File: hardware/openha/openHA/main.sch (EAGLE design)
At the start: 58 parts, among them U1 STM32L476JX, U2 PCM1774RGPR, U3 STC3115IQT, X1 ABS06-107SMT, X2 ABS06-107SMT

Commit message: Initial corrections
Miscellaneous corrections of the initial commit
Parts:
- removed U$1: BATT, STM32:BATT
- removed U$15: BLUENRG-MS, STM32:BLUENRG-MS
- removed U$16: BALF-NRG-01D3, STM32:BALF-NRG-01D3
- removed U$17: ANT, STM32:ANT
- removed U$18, U$19: 2k, STM32:RESISTOR
- removed U$2: USB, STM32:USB
- removed U$3: LD5115J18, STM32:LD5115J18
- removed U$4: STBC08, STM32:STBC08
- removed U$5: USBLC6-2, STM32:USBLC6-2
- removed U$7: MP34DT05-A, STM32:MP34DT05-A
- removed U$8: LDK130, STM32:LDK130
- removed X1, X2: ABS06-107SMT, STM32:ABS06-107SMT
- added A1: ANT, OAlib:ANT
- added C37, C38: 4.7uF, OAlib:CAP0603
- added J1: 2PIN, OAlib:2PIN
- added J2: BATT, OAlib:BATT
- added J3: CS44, OAlib:CS44
- added L2: 3.9NH, SparkFun-Coils:INDUCTOR-0402-3.9NH
- added R3: 2k, OAlib:RESISTOR
- added R4: 0R, OAlib:RESISTOR
- added R5: 20k, OAlib:RESISTOR
- added S2: SW_DPDT, OAlib:SW_DPDT
- added U10: STBC08, OAlib:STBC08
- added U4: PCM1774RGPR, PCM1774:PCM1774RGPR
- added U5: BLUENRG-MS, OAlib:BLUENRG-MS
- added U6: LD39115J18, OAlib:LD39115J18
- added U7: STC3115IQT, STC3115IQT:STC3115IQT
- added U8: USBLC6-2, OAlib:USBLC6-2
- added U9: LDK130, OAlib:LDK130
- added Y1, Y2: ABS06-107SMT, OAlib:ABS06-107SMT
- C1, C11, C12, C17, C18, C19, C21, C22, C23, C24, C25, C3, C7, C8: device STM32:CAP0603 -> OAlib:CAP0603
- C10, C34, C6, C9: value 4.7uF -> 1uF; device STM32:CAP0603 -> OAlib:CAP0603
- C13: value 1uF -> 100nF; device STM32:CAP0603 -> OAlib:CAP0603
- C14, C15, C16: value 1uF -> 4.7uF; device STM32:CAP0603 -> OAlib:CAP0603
- C2: value 4pF -> 1uF; device STM32:CAP0603 -> OAlib:CAP0603
- C20: value 4.7uF -> 100pF; device STM32:CAP0603 -> OAlib:CAP0603
- C26: value 150nF -> 15pF; device STM32:CAP0603 -> OAlib:CAP0603
- C27: value 100p -> 150nF; device STM32:CAP0603 -> OAlib:CAP0603
- C28: value 100nF -> 100p; device STM32:CAP0603 -> OAlib:CAP0603
- C29: value 1uF -> 15pF; device STM32:CAP0603 -> OAlib:CAP0603
- C30: value 100pF -> 100nF; device STM32:CAP0603 -> OAlib:CAP0603
- C31, C4: value 100nF -> 1uF; device STM32:CAP0603 -> OAlib:CAP0603
- C32: value 1uF -> 4pF; device STM32:CAP0603 -> OAlib:CAP0603
- C33, C5: value 4.7uF -> 100nF; device STM32:CAP0603 -> OAlib:CAP0603
- C35, C36: value 15pF -> 4.7uF; device STM32:CAP0603 -> OAlib:CAP0603
- L1: value 3.9NH -> BALF-NRG-01D3; device SparkFun-Coils:INDUCTOR-0402-3.9NH -> OAlib:BALF-NRG-01D3
- R1: value 20k -> 2k; device STM32:RESISTOR -> OAlib:RESISTOR
- R2: device STM32:RESISTOR -> OAlib:RESISTOR
- U1: device STM32:STM32L476JX -> OAlib:STM32L476JX
- U2: value PCM1774RGPR -> MP34DT05-A; device PCM1774:PCM1774RGPR -> OAlib:MP34DT05-A
- U3: value STC3115IQT -> MP34DT05-A; device STC3115IQT:STC3115IQT -> OAlib:MP34DT05-A
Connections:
- removed net GG_SCL: U3.SCL
- removed net GG_SDA: U1.PB15, U3.SDA
- removed net GPIO2: U1.PC1, U2.MD/SDA
- removed net GPIO3: U1.PC0, U2.MC/SCL
- removed net MIC_CLK: U$7.CLK, U1.PC2
- removed net MIC_DATA: U$7.DOUT, U1.PB6
- removed net RXD-USB_DM: U$5.I1
- removed net SAI_FS: U2.LRCK
- removed net SAI_MCLK: U2.BCK
- removed net VDD: C12.1, C13.1, C14.1, C15.1, C16.1, C22.1, C23.1, C24.1, C25.1, C26.1, C27.1, C28.2, C29.2, C3.1, C30.1, C31.1, C32.1, C7.1, C8.1, U$15.VBAT1, U$15.VBAT3, U$15.VDD1V2, U$15.VDD1V8, U$3.OUT, U$7.VDD, U1.VBAT, U1.VDD, U1.VDDA, U1.VDD_2, U1.VDD_3, U1.VREF+
- new net 1V8: C10.1, C11.1, C12.1, C2.1, C20.1, C21.1, C22.1, C23.1, C24.1, C25.1, C27.1, C28.1, C30.2, C31.2, C32.1, C4.1, C5.1, C6.1, C7.1, C8.1, C9.1, U1.VBAT, U1.VDD, U1.VDDA, U1.VDD_2, U1.VDD_3, U1.VREF+, U2.VDD, U3.VDD, U5.VBAT1, U5.VBAT3, U5.VDD1V2, U5.VDD1V8, U6.OUT
- new net I2C_SCL: U1.PC0, U4.MC/SCL, U7.SCL
- new net I2C_SDA: U1.PC1, U4.MD/SDA, U7.SDA
- new net MIC1_CLK: U1.PC2, U2.CLK
- new net MIC1_DATA: U1.PB6, U2.DOUT
- new net MIC2_CLK: U1.PB11, U3.CLK
- new net MIC2_DATA: U1.PB10, U3.DOUT
- new net N$20: U1.PA10
- new net SAI_BCK: U1.PG11, U4.BCK
- new net SAI_LR: U1.PG10, U4.LRCK
- new net SWDCLK: S2.4, U1.PA14
- new net SWDIO: S2.1, U1.PA13
- new net TXD-USB_DM: U1.PA11, U8.I1
- new net USB_DM: S2.6, U8.O1
- new net USB_DP: S2.3, U8.O2
- net 3V3: now also C13.2, C14.2, C15.2, C16.2, C17.2, C36.1, R4.2, U4.MODE, U4.VCC, U4.VCOM, U4.VDD, U4.VIO, U4.VPA, U9.OUT; no longer C19.2, C20.2, C21.2, C34.1, C5.2, C6.2, U$8.OUT, U2.MODE, U2.VCC, U2.VCOM, U2.VDD, U2.VIO, U2.VPA
- net BAT_NTC: now also J2.NTC, U7.BATD/CD; no longer U$1.2, U3.BATD/CD
- net BLUE_CLK: now also U5.SPI_CLK; no longer U$15.SPI_CLK
- net BLUE_CS: now also U5.SPI_CS; no longer U$15.SPI_CS
- net BLUE_IRQ: now also U5.SPI_IRQ; no longer U$15.SPI_IRQ
- net BLUE_MISO: now also U5.SPI_MISO; no longer U$15.SPI_MISO
- net BLUE_MOSI: now also U5.SPI_MOSI; no longer U$15.SPI_MOSI
- net CHRG: now also D2.K2, U10.CHRG; no longer D1.K2, U$4.CHRG
- net GND: now also A1.P$2, C11.2, C13.1, C14.1, C15.1, C16.1, C17.1, C20.2, C21.2, C28.2, C36.2, C37.2, C38.2, C5.2, C6.2, D1.K2, J2.BAT-, J3.4, L1.GND, L2.2, R5.2, U10.GND, U10.PAD, U2.GND, U2.LR, U3.LR, U4.AGND, U4.DGND, U4.EPAD, U4.MS/ADR, U4.PGND, U5.GND_1, U5.GND_2, U5.GND_3, U5.SMPS-GND, U5.TEST10, U5.TEST11, U5.TEST12, U5.TEST2, U5.TEST3, U5.TEST4, U5.TEST5, U5.TEST6, U5.TEST7, U5.TEST8, U5.TEST9, U6.GND, U7.GND, U8.GND, U9.GND; no longer C13.2, C14.2, C15.2, C16.2, C19.1, C20.1, C21.1, C30.2, C31.2, C34.2, C5.1, C6.1, D2.K2, L1.2, R1.2, U$1.3, U$15.GND_1, U$15.GND_2, U$15.GND_3, U$15.SMPS-GND, U$15.TEST10, U$15.TEST11, U$15.TEST12, U$15.TEST2, U$15.TEST3, U$15.TEST4, U$15.TEST5, U$15.TEST6, U$15.TEST7, U$15.TEST8, U$15.TEST9, U$16.GND, U$17.P$2, U$2.SH1, U$2.SH2, U$3.GND, U$4.GND, U$5.GND, U$7.GND, U$7.LR, U$8.GND, U2.AGND, U2.DGND, U2.EPAD, U2.MS/ADR, U2.PGND
- net HPL: now also J1.1
- net HPR: now also C19.2, J1.2; no longer C17.2
- net N$1: now also R1.1, U1.PB7; no longer U$19.1, U1.PB3
- net N$10: now also C19.1, U4.HPOR/LOR; no longer C17.1, U2.HPOR/LOR
- net N$11: now also J3.3, S2.2; no longer U$2.3, U$5.O2
- net N$12: now also A1.P$1, L1.ANT; no longer U$16.ANT, U$17.P$1
- net N$13: now also L1.RX_P, U5.RF1; no longer U$15.RF1, U$16.RX_P
- net N$14: now also L1.RX_N, U5.RF0; no longer U$15.RF0, U$16.RX_N
- net N$15: now also D1.A2, R1.2; no longer D2.A2, U$19.2
- net N$19: now also C30.1, C31.1, U5.SMPSFILT2; no longer C28.1, C29.1, U$15.SMPSFILT2
- net N$2: now also C29.2, L2.1; no longer C36.2, L1.1
- net N$3: now also U4.HPOL/LOL; no longer U2.HPOL/LOL
- net N$6: now also D2.A2, R3.2; no longer D1.A2, U$18.2
- net N$7: now also C34.2, U7.CG; no longer C11.2, U3.CG
- net N$8: now also R5.1, U10.PROG; no longer R1.1, U$4.PROG
- net N$9: now also J3.2, S2.5; no longer U$2.2, U$5.O1
- net OSC_BLUE_IN: now also C26.1, U5.FXTAL1, Y2.P$1; no longer C35.1, U$15.FXTAL1, X2.P$1
- net OSC_BLUE_OUT: now also C29.1, U5.FXTAL0, Y2.P$2; no longer C36.1, U$15.FXTAL0, X2.P$2
- net OSC_IN: now also Y1.P$1; no longer X1.P$1
- net OSC_OUT: now also C3.1, Y1.P$2; no longer C2.1, X1.P$2
- net RXD-USB_DP: now also U1.PA12, U8.I2; no longer U$5.I2
- net SAI_SCK: now also U1.PG9, U4.SCKI; no longer U2.SCKI
- net SAI_SD: now also U1.PG12, U4.DIN; no longer U2.DIN
- net VBAT: now also C34.1, C35.1, C38.1, J2.BAT+, U10.BAT, U6.EN, U6.IN, U7.VCC, U7.VIN, U9.IN; no longer C11.1, C33.1, C9.1, U$1.1, U$3.EN, U$3.IN, U$4.BAT, U$8.IN, U3.VCC, U3.VIN
- net VDDUSB: now also R4.1
- net V_USB: now also C33.1, C37.1, J3.1, R3.1, U10.VCC, U8.VBUS; no longer C10.1, C4.1, U$18.1, U$2.1, U$4.VCC, U$5.VBUS
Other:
- note added: "Max 150mA"
- note added: "Max 300mA"
- note removed: "VDD = 1.8V"

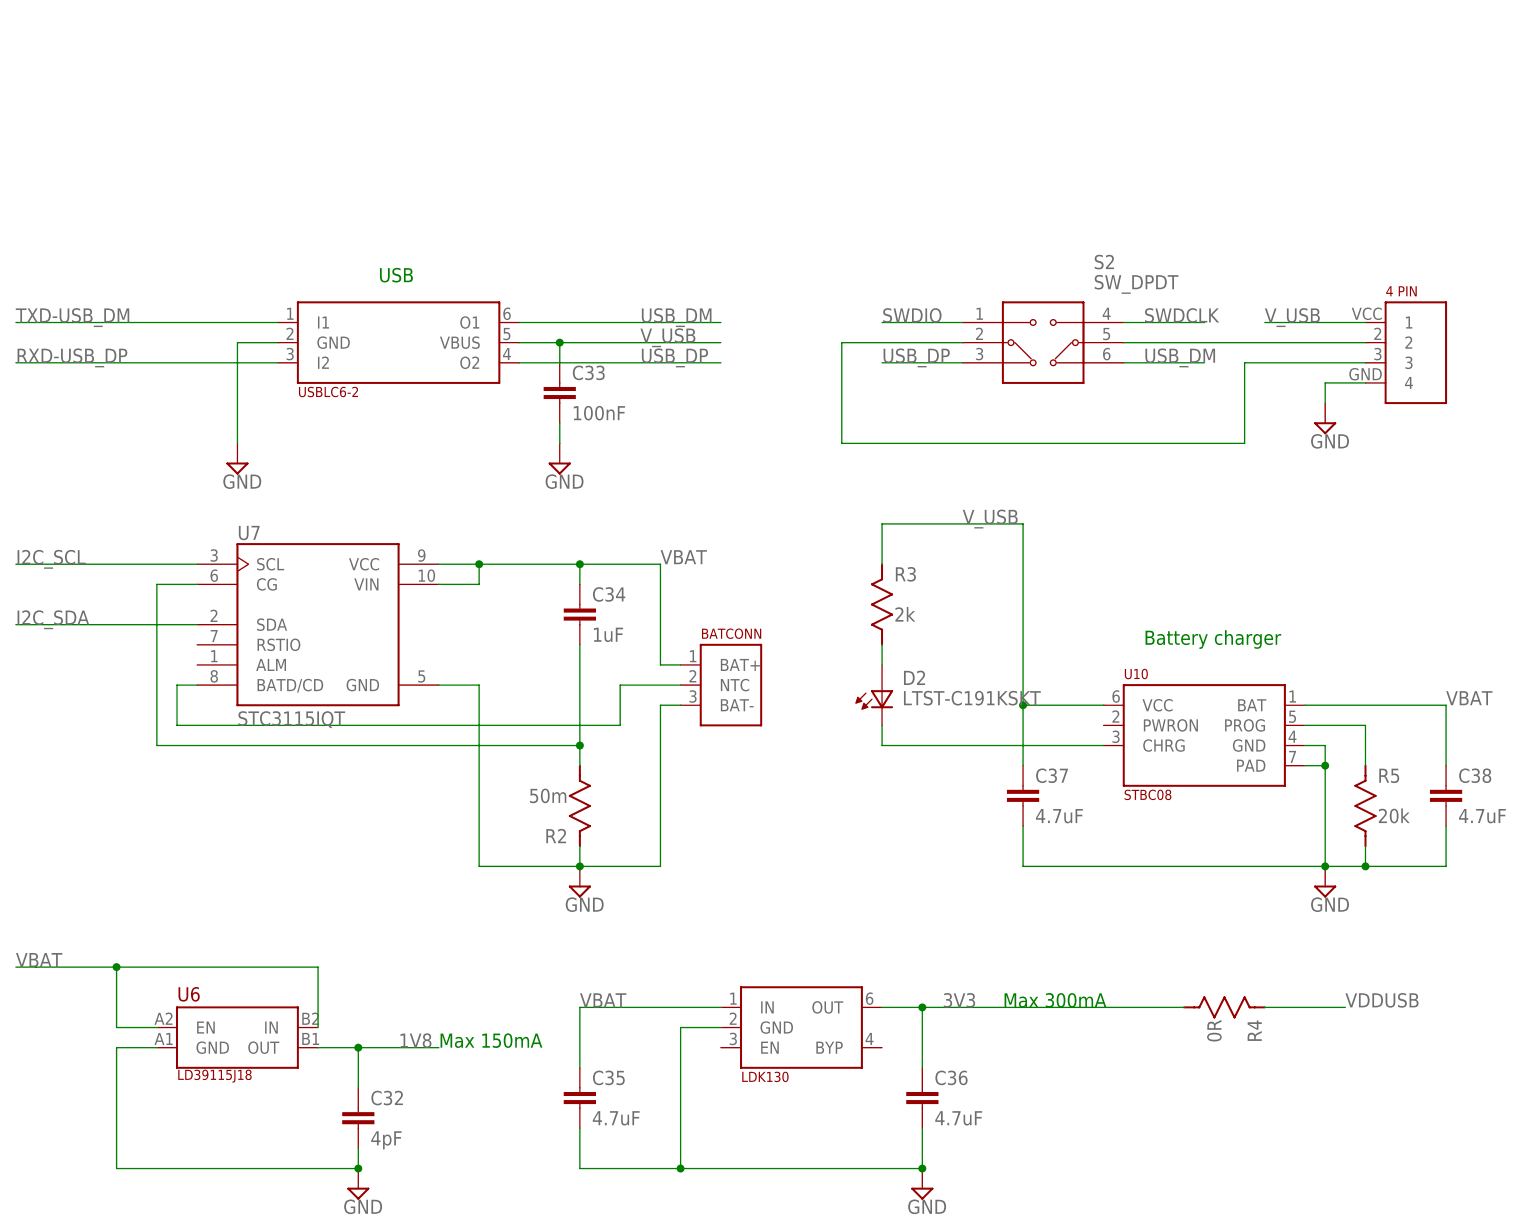
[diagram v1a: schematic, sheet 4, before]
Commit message: Various BOM update
Replace 4pin micro connector by USB (used for USB and SWD)
Update BOM for LED, Crystal, Self and 3V3 LDO
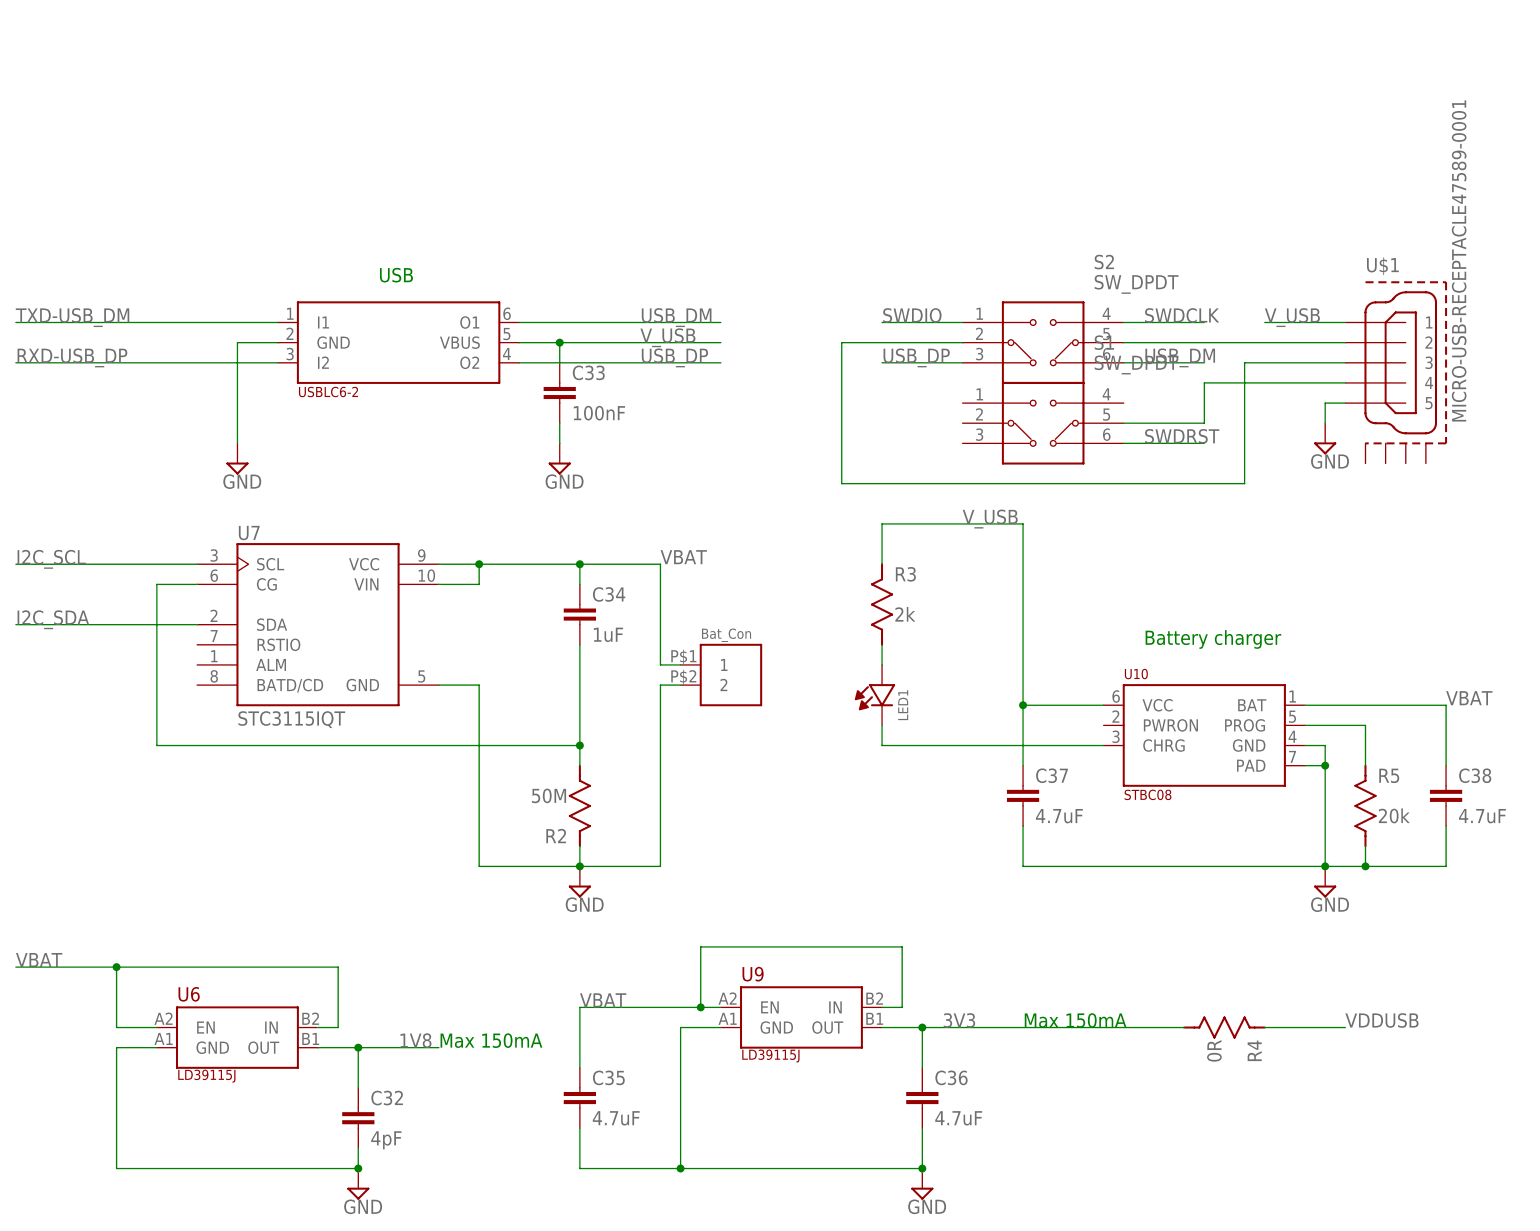
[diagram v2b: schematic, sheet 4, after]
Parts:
- removed D1, D2: LTST-C191KSKT, LTST-C191KSKT:LTST-C191KSKT
- removed J2: BATT, OAlib:BATT
- removed L2: 3.9NH, SparkFun-Coils:INDUCTOR-0402-3.9NH
- removed Y2: ABS06-107SMT, OAlib:ABS06-107SMT
- added L3: 3.9nH, OAlib:L
- added LED1, LED2: (no value), OAlib:LED-KPG-0603
- added S1: SW_DPDT, OAlib:SW_DPDT
- added U$1: MICRO-USB-RECEPTACLE47589-0001, OAlib:MICRO-USB-RECEPTACLE47589-0001
- added U$2: 32MHz, OAlib:ABM11W-101
- J1: value 2PIN -> HP_Con
- J3: value CS44 -> Bat_Con; device OAlib:CS44 -> OAlib:2PIN
- R2: value 50m -> 50M
- U6: value LD39115J18 -> LD39115J; device OAlib:LD39115J18 -> OAlib:LD39115J
- U9: value LDK130 -> LD39115J; device OAlib:LDK130 -> OAlib:LD39115J
- Y1: value ABS06-107SMT -> 32.768kHz; device OAlib:ABS06-107SMT -> OAlib:ABS06-107
- renumbered U1 to U11
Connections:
- removed net BAT_NTC: J2.NTC, U7.BATD/CD
- new net N$16: S1.5, U$1.4
- new net SWDRST: S1.6, U11.NRST
- net CHRG: now also LED1.K; no longer D2.K2
- net GND: now also J3.2, L3.2, LED2.K, U$1.5, U$2.P$2, U$2.P$4; no longer D1.K2, J2.BAT-, J3.4, L2.2
- net N$11: now also U$1.3; no longer J3.3
- net N$15: now also LED2.A; no longer D1.A2
- net N$2: now also L3.1; no longer L2.1
- net N$6: now also LED1.A; no longer D2.A2
- net N$9: now also U$1.2; no longer J3.2
- net OSC_BLUE_IN: now also U$2.P$1; no longer Y2.P$1
- net OSC_BLUE_OUT: now also U$2.P$3; no longer Y2.P$2
- net VBAT: now also J3.1, U9.EN; no longer J2.BAT+
- net V_USB: now also U$1.1; no longer J3.1
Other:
- note removed: "Max 300mA"
- moved on the sheet: R4
